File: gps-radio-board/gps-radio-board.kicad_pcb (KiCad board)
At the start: 4 copper layers, 25 x 54 mm, 45 parts, among them J1 SMA, J2 SMA, J3 USB_C_Receptacle_USB2.0_16P, J4 JST_BATT, J5 Conn_01x04, J6 Conn_01x04, J7 Conn_01x04, U1 ESP32-C6-MINI-1U-H4, U4 AP2112K-3.3, U5 MAX-M10N, U6 MCP73831, U7 AP2112K-3.3

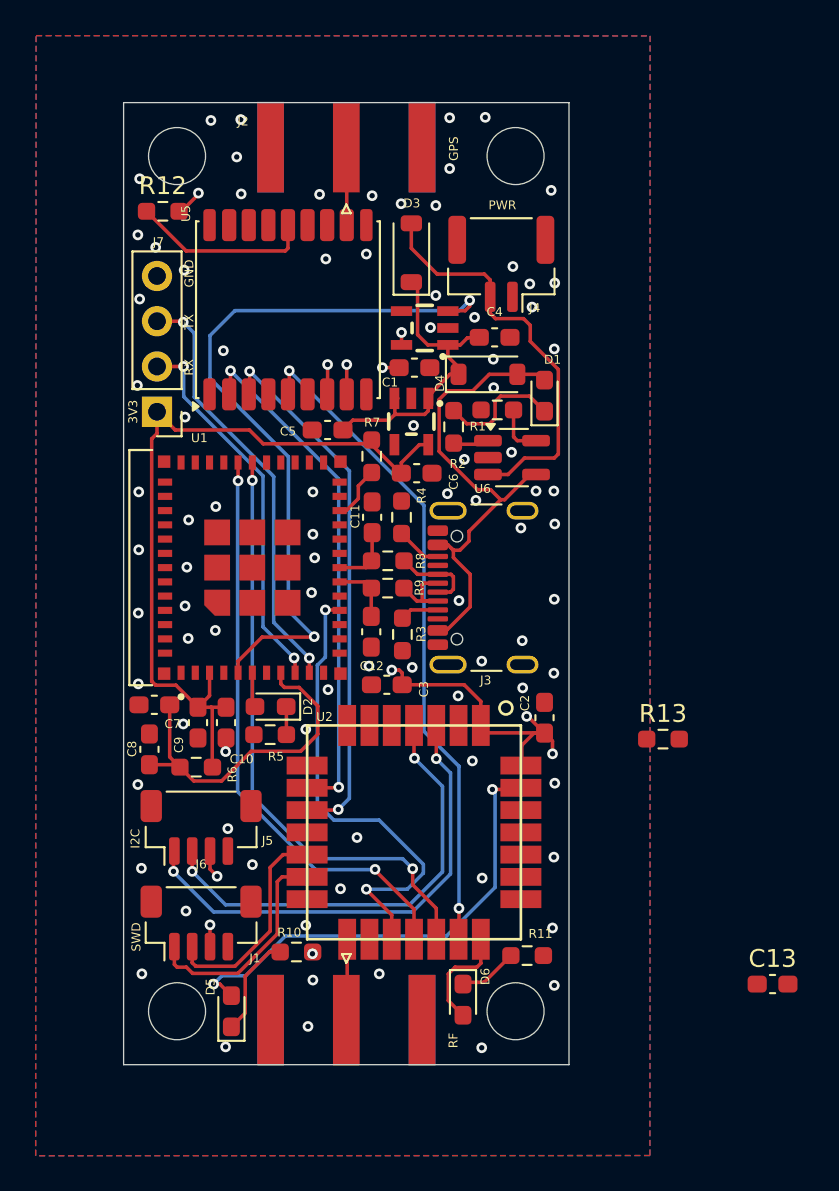
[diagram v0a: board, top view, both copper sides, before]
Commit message: Routing, mostly finished
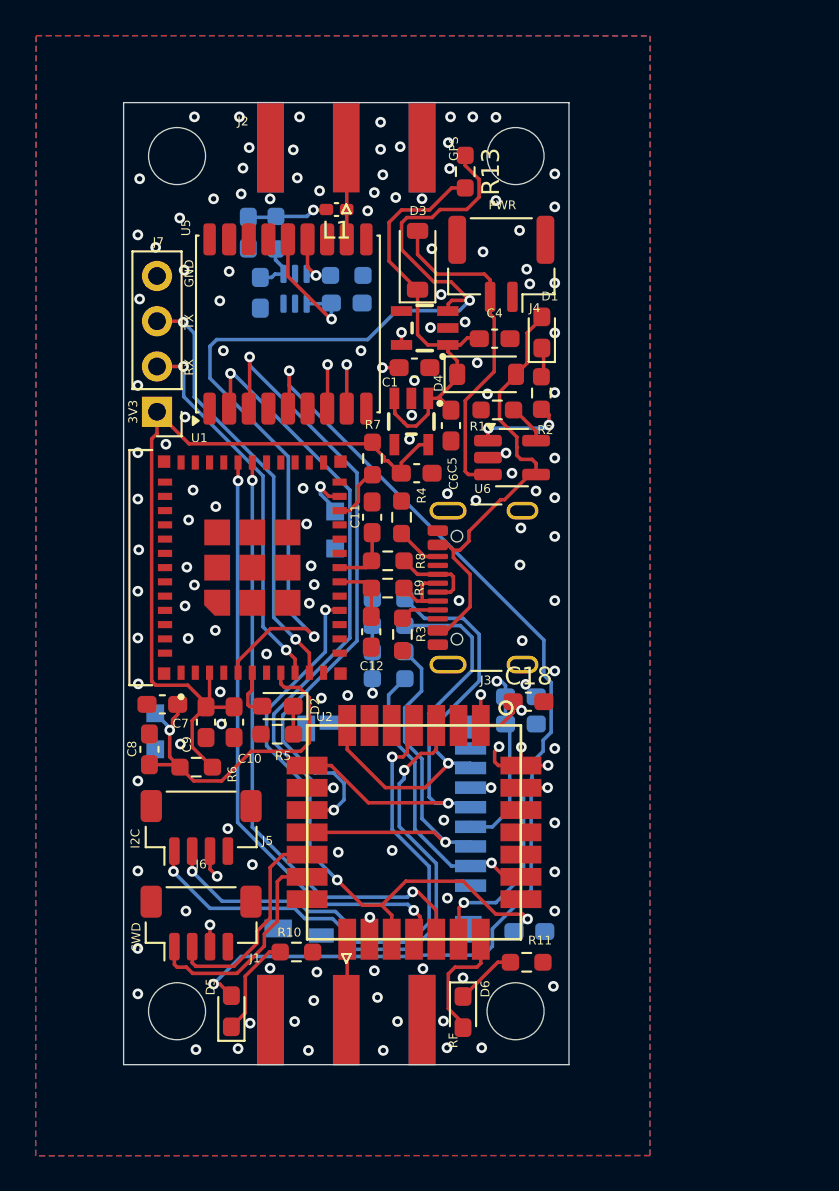
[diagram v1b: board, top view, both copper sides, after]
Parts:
- removed C2: 100n, Capacitor_SMD:C_0603_1608Metric_Pad1.08x0.95mm_HandSolder
- removed C3: 10u, Capacitor_SMD:C_0603_1608Metric_Pad1.08x0.95mm_HandSolder
- removed R12: 0, Resistor_SMD:R_0603_1608Metric_Pad0.98x0.95mm_HandSolder
- added BOOT1: TP2, TestPoint:TestPoint_Pad_1.0x1.0mm, B.Cu at (99.4, 96.0)
- added C14: 100n, Capacitor_SMD:C_0603_1608Metric_Pad1.08x0.95mm_HandSolder, B.Cu at (95.2, 83.7)
- added C15: 1u, Capacitor_SMD:C_0603_1608Metric_Pad1.08x0.95mm_HandSolder, B.Cu at (100.0, 84.2)
- added C16: 10n, Capacitor_SMD:C_0603_1608Metric_Pad1.08x0.95mm_HandSolder, B.Cu at (94.5, 80.3)
- added C17: 10u, Capacitor_SMD:C_0603_1608Metric_Pad1.08x0.95mm_HandSolder, B.Cu at (109.8, 106.3)
- added C18: 4.7u, Capacitor_SMD:C_0603_1608Metric_Pad1.08x0.95mm_HandSolder, F.Cu at (110.2, 106.6)
- added C19: 100n, Capacitor_SMD:C_0603_1608Metric_Pad1.08x0.95mm_HandSolder, B.Cu at (109.8, 107.9)
- added EN1: ESP_EN, TestPoint:TestPoint_Pad_1.0x1.0mm, B.Cu at (89.3, 109.3)
- added EN2: ESP_EN, TestPoint:TestPoint_Pad_1.0x1.0mm, B.Cu at (89.3, 107.3)
- added GND1: TP2, TestPoint:TestPoint_Pad_1.0x1.0mm, B.Cu at (99.4, 98.0)
- added J8: DM3CS-SF, Connector_Card:microSD_HC_Hirose_DM3D-SF, B.Cu at (101.6, 113.8)
- added L1: 27n, Inductor_SMD:L_0402_1005Metric_Pad0.77x0.64mm_HandSolder, F.Cu at (99.5, 79.0)
- added R14: 100k, Resistor_SMD:R_0603_1608Metric_Pad0.98x0.95mm_HandSolder, B.Cu at (100.0, 82.7)
- added R15: 10, Resistor_SMD:R_0603_1608Metric_Pad0.98x0.95mm_HandSolder, B.Cu at (96.0, 80.3)
- added R16: 10k, Resistor_SMD:R_0603_1608Metric_Pad0.98x0.95mm_HandSolder, B.Cu at (102.4, 105.3)
- added R17: 10k, Resistor_SMD:R_0603_1608Metric_Pad0.98x0.95mm_HandSolder, B.Cu at (102.4, 103.8)
- added R18: 10k, Resistor_SMD:R_0603_1608Metric_Pad0.98x0.95mm_HandSolder, B.Cu at (102.4, 100.8)
- added R19: 10k, Resistor_SMD:R_0603_1608Metric_Pad0.98x0.95mm_HandSolder, B.Cu at (102.4, 102.3)
- added U3: SiP32431DR3, Package_TO_SOT_SMD:SOT-363_SC-70-6, B.Cu at (97.1, 83.5)
- C13: moved to B.Cu
- moved R13 33.7 mm to (106.7, 76.9), turned to -90 degrees
- moved C13 14.0 mm to (110.3, 119.5)
- moved C5 6.93 mm to (105.9, 91.1), turned to -90 degrees
- moved R2 5.28 mm to (111.0, 89.3)
- moved D1 3.55 mm to (111.0, 85.9)
- moved U5 0.80 mm to (96.7, 85.4)
- moved D6 0.70 mm to (106.5, 124.0)
- moved D3 0.55 mm to (104.0, 81.8)
- moved C10 0.45 mm to (93.7, 107.8)
- moved C7 0.45 mm to (89.7, 106.8)
- moved C9 0.45 mm to (92.1, 107.8)
- moved D2 0.40 mm to (96.2, 106.9)
- moved R5 0.40 mm to (96.1, 108.5)
- moved R11 0.38 mm to (110.1, 121.2)
- moved R7 0.13 mm to (101.5, 93.0)
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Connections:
- U1 pad 23: unconnected-(U1-IO9-Pad23) -> Net-(U1-IO9)
- U2 pad 25: Net-(U2-PB9) -> unconnected-(U2-PB9-Pad25)
- U5 pad 13: Net-(U2-PB9) -> Net-(U3-ON)
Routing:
- net /SPI-SCK: track 0.00 -> 25.3 mm, vias 0 -> 1
- net /SPI-CITO: track 0.00 -> 23.3 mm, vias 0 -> 1
- net /SPI-COTI: track 0.00 -> 22.2 mm, vias 0 -> 1
- net /SPI-CS: track 0.00 -> 16.6 mm, vias 0 -> 1
- net Net-(U1-IO2): track 41.9 -> 56.2 mm
- net +3V3: track 26.2 -> 34.9 mm, vias 10 -> 13
- net Net-(U1-IO6): track 26.7 -> 34.9 mm, vias 2 -> 3
- net Net-(D3-K): track 18.7 -> 25.2 mm
- net /EXT_INT_GPS: track 37.2 -> 42.5 mm
- net Net-(D1-K): track 6.95 -> 1.62 mm
- net /WIO_UART_1_TX: track 30.2 -> 35.6 mm
- net /SWD-WIO-IO: track 27.1 -> 31.9 mm
- net Net-(C16-Pad2): track 0.00 -> 4.58 mm, vias 0 -> 1
- net +BATT: track 23.3 -> 18.9 mm
- net /SWD-WIO-CLK: track 25.6 -> 29.7 mm
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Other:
- board text added: "BOOT"
- board text added: "RST"

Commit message: Finish routing
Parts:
- moved C18 1.16 mm to (111.2, 107.3), turned to -90 degrees
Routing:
- net +3V3: track 34.9 -> 38.6 mm, vias 13 -> 14
- net +BATT: track 18.9 -> 21.0 mm
- net /EXT_INT_GPS: track 42.5 -> 43.2 mm
- net GND: vias 131 -> 135

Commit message: Small adjustments
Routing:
- net +3V3: track 38.6 -> 36.3 mm
- net Net-(U1-IO6): track 34.9 -> 35.6 mm
- net Net-(D3-K): track 25.2 -> 25.7 mm
- net GND: vias 135 -> 136

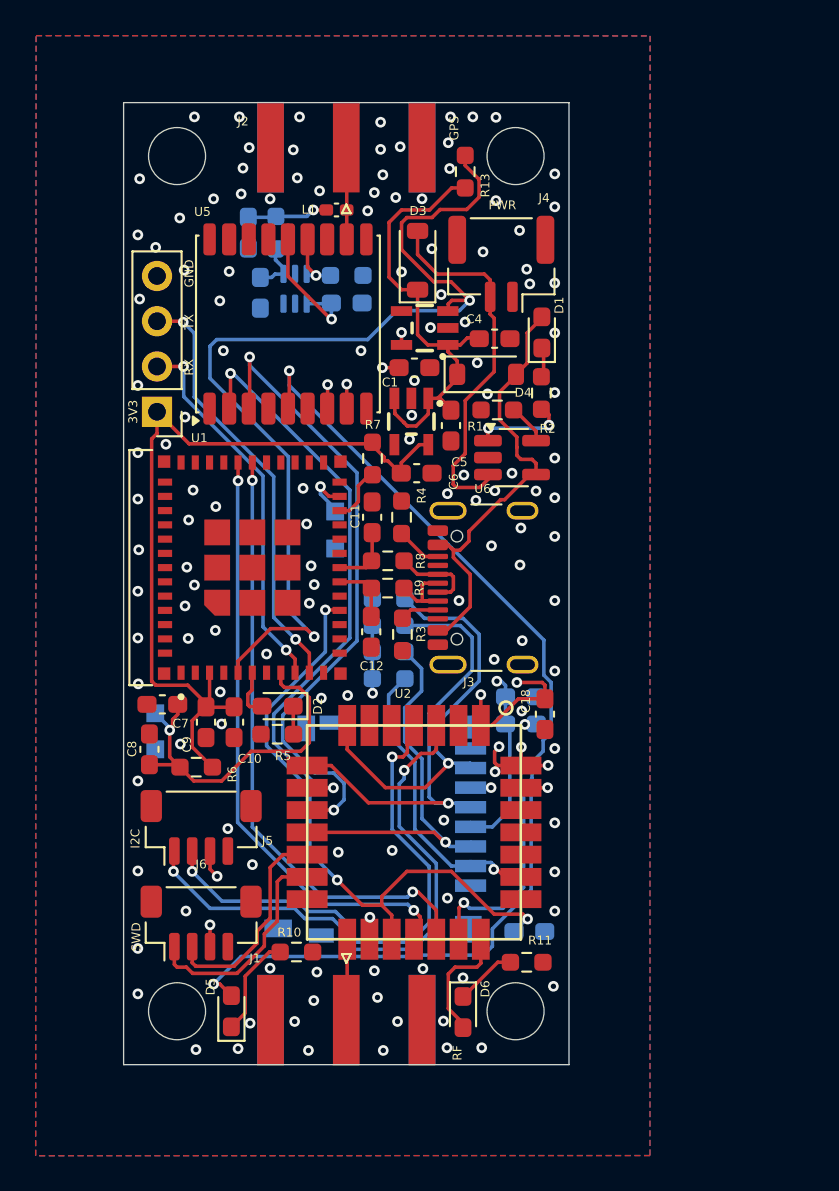
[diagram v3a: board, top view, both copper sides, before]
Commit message: Layout fixes. Swap 100k ref for en
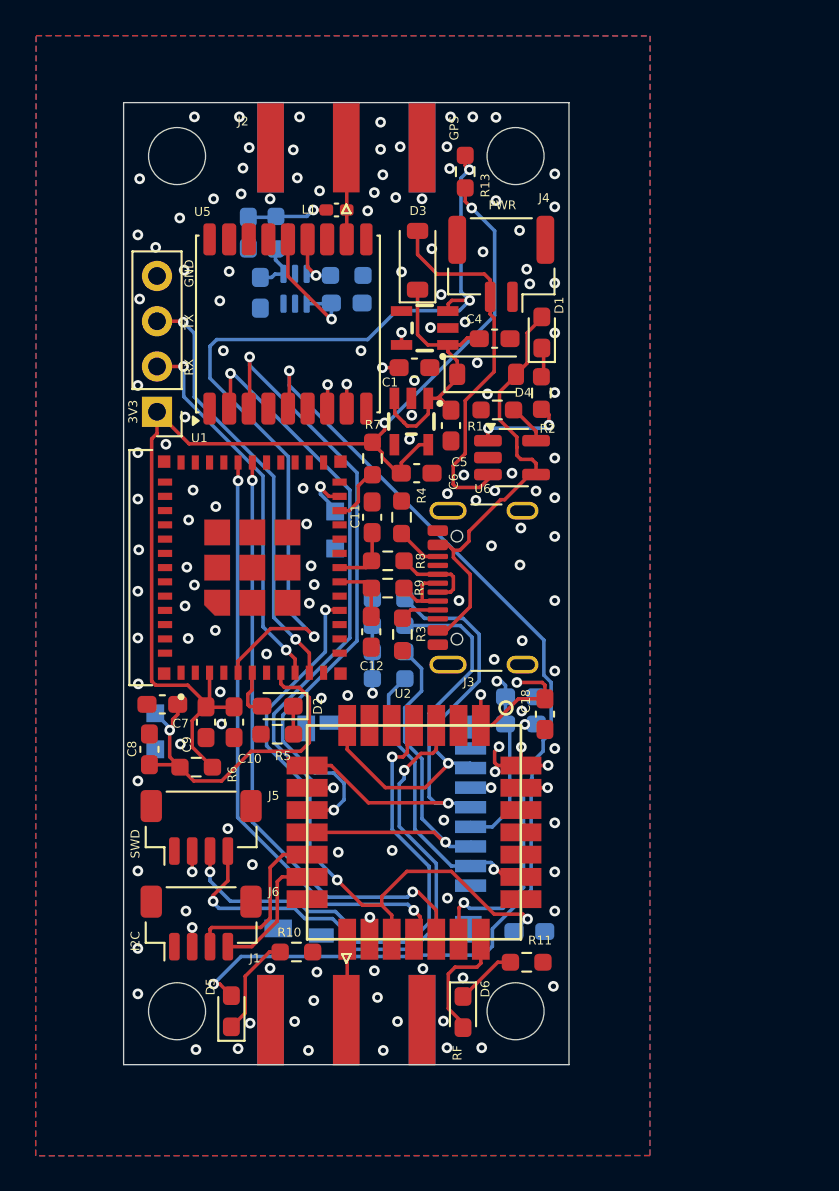
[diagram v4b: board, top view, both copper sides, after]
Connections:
- J5 pad 1: /SWD-WIO-IO -> GND
- J5 pad 2: /SWD-WIO-CLK -> +3V3
- J5 pad 3: +3V3 -> /SWD-WIO-CLK
- J5 pad 4: GND -> /SWD-WIO-IO
- J6 pad 1: /I2C-2-SCL -> GND
- J6 pad 2: /I2C-2-SCA -> +3V3
- J6 pad 3: +3V3 -> /I2C-2-SCA
- J6 pad 4: GND -> /I2C-2-SCL
- R13 pad 2: Net-(D3-K) -> +3V3_E
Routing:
- net +3V3_E: track 43.7 -> 61.7 mm, vias 0 -> 2
- net Net-(D3-K): track 25.7 -> 15.7 mm
- net Net-(U1-IO2): track 56.2 -> 50.7 mm, vias 2 -> 3
- net /I2C-2-SCL: track 12.6 -> 7.37 mm
- net /I2C-2-SCA: track 11.8 -> 9.83 mm
- net /SWD-WIO-IO: track 31.9 -> 31.1 mm
- net /SWD-WIO-CLK: track 29.7 -> 29.1 mm
- net +3V3: track 36.3 -> 35.7 mm

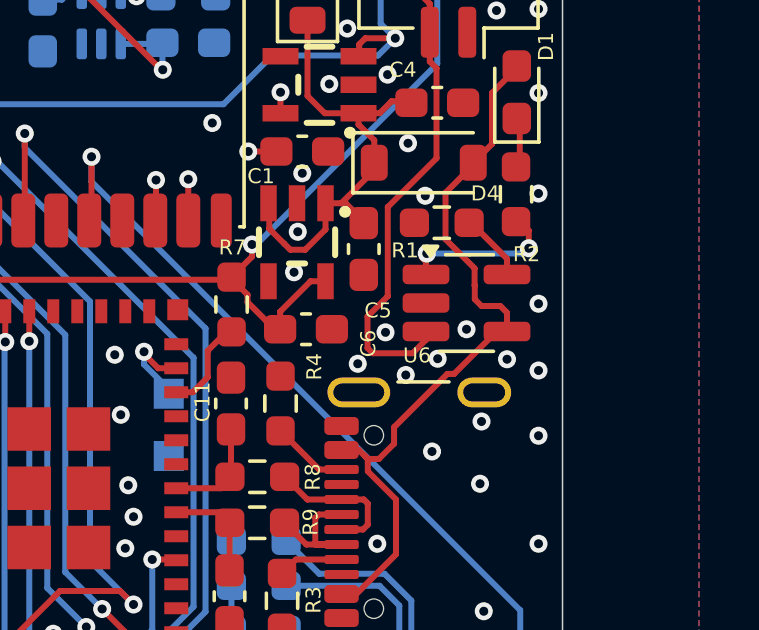
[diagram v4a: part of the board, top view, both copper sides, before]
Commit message: Add output cap for battery charger
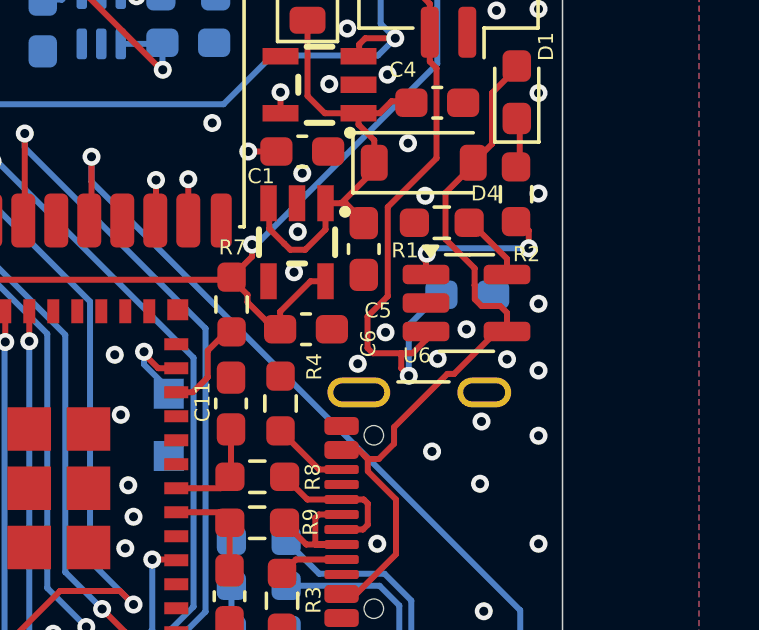
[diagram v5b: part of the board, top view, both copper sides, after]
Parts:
- added C20: 4.7u, Capacitor_SMD:C_0603_1608Metric_Pad1.08x0.95mm_HandSolder, B.Cu at (109.3, 92.7)
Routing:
- net +BATT: track 21.0 -> 25.1 mm, vias 0 -> 1
- net GND: vias 136 -> 135
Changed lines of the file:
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@@
 			(outputformat 1)
 			(mirror no)
-			(drillshape 1)
+			(drillshape 0)
 			(scaleselection 1)
-			(outputdirectory "")
+			(outputdirectory "gps-gerb/")
 		)
 	)
@@
 	(footprint "Capacitor_SMD:C_0603_1608Metric_Pad1.08x0.95mm_HandSolder"
 		(layer "B.Cu")
+		(at 109.325 92.65)
+		(descr "Capacitor SMD 0603 (1608 Metric), square (rectangular) end terminal, IPC-7351 nominal with elongated pad for handsoldering. (Body size source: IPC-SM-782 page 76, https://www.pcb-3d.com/wordpress/wp-content/uploads/ipc-sm-782a_amendment_1_and_2.pdf)")
+		(tags "capacitor handsolder")
+		(property "Reference" "C20"
+			(at 0.025 1.125 0)
+			(layer "B.SilkS")
+			(effects
+				(font
+					(size 0.5 0.5)
+					(thickness 0.07)
+				)
+				(justify mirror)
+			)
+		)
+		(property "Value" "4.7u"
+			(at 0 -1.43 0)
+			(layer "B.Fab")
+			(effects
+				(font
+					(size 1 1)
+					(thickness 0.15)
+				)
+				(justify mirror)
+			)
+		)
+		(property "Datasheet" ""
+			(at 0 0 0)
+			(layer "B.Fab")
+			(hide yes)
+			(effects
+				(font
+					(size 1.27 1.27)
+				)
+				(justify mirror)
+			)
+		)
+		(property "Description" "Unpolarized capacitor"
+			(at 0 0 0)
+			(layer "B.Fab")
+			(hide yes)
+			(effects
+				(font
+					(size 1.27 1.27)
+				)
+				(justify mirror)
+			)
+		)
+		(property ki_fp_filters "C_*")
+		(sheetname "/")
+		(sheetfile "gps-radio-board.kicad_sch")
+		(units
+			(unit
+				(name "A")
+				(pins "1" "2")
+			)
+		)
+		(attr smd)
+		(duplicate_pad_numbers_are_jumpers no)
+		(fp_line
+			(start -0.146267 -0.51)
+			(end 0.146267 -0.51)
+			(stroke
+				(width 0.12)
+				(type solid)
+			)
+			(layer "B.SilkS")
+		)
+		(fp_line
+			(start -0.146267 0.51)
+			(end 0.146267 0.51)
+			(stroke
+				(width 0.12)
+				(type solid)
+			)
+			(layer "B.SilkS")
+		)
+		(fp_rect
+			(start -1.65 0.73)
+			(end 1.65 -0.73)
+			(stroke
+				(width 0.05)
+				(type solid)
+			)
+			(fill no)
+			(layer "B.CrtYd")
+		)
+		(fp_rect
+			(start -0.8 0.4)
+			(end 0.8 -0.4)
+			(stroke
+				(width 0.1)
+				(type solid)
+			)
+			(fill no)
+			(layer "B.Fab")
+		)
+		(fp_text user "${REFERENCE}"
+			(at 0 0 0)
+			(layer "B.Fab")
+			(effects
+				(font
+					(size 0.4 0.4)
+					(thickness 0.06)
+				)
+				(justify mirror)
+			)
+		)
+		(pad "1" smd roundrect
+			(at -0.8625 0)
+			(size 1.075 0.95)
+			(layers "B.Cu" "B.Mask" "B.Paste")
+			(roundrect_rratio 0.25)
+			(net "+BATT")
+			(pintype "passive")
+		)
+		(pad "2" smd roundrect
+			(at 0.8625 0)
+			(size 1.075 0.95)
+			(layers "B.Cu" "B.Mask" "B.Paste")
+			(roundrect_rratio 0.25)
+			(net "GND")
+			(pintype "passive")
+		)
+		(embedded_fonts no)
+		(model "${KICAD10_3DMODEL_DIR}/Capacitor_SMD.3dshapes/C_0603_1608Metric.step"
+			(offset
+				(xyz 0 0 0)
+			)
+			(scale
+				(xyz 1 1 1)
+			)
+			(rotate
+				(xyz 0 0 0)
+			)
+		)
+	)
+	(footprint "Capacitor_SMD:C_0603_1608Metric_Pad1.08x0.95mm_HandSolder"
+		(layer "B.Cu")
 		(at 109.8 107.875)
 		(descr "Capacitor SMD 0603 (1608 Metric), square (rectangular) end terminal, IPC-7351 nominal with elongated pad for handsoldering. (Body size source: IPC-SM-782 page 76, https://www.pcb-3d.com/wordpress/wp-content/uploads/ipc-sm-782a_amendment_1_and_2.pdf)")
@@
 	)
 	(via
-		(at 107.275 95.325)
-		(size 0.6)
-		(drill 0.3)
-		(layers "F.Cu" "B.Cu")
-		(free yes)
-		(net "GND")
-	)
-	(via
 		(at 88.3 116.125)
 		(size 0.6)
@@
 	)
 	(segment
-		(start 111.15 91.275)
+		(start 108.15 91.1)
 		(end 111.325 91.1)
 		(width 0.2)
@@
 	(segment
 		(start 107.975 91.275)
-		(end 111.15 91.275)
+		(end 108.15 91.1)
 		(width 0.2)
 		(layer "B.Cu")
@@
 	)
 	(segment
+		(start 106.173529 94.6)
+		(end 107.125 94.6)
+		(width 0.2)
+		(layer "F.Cu")
+		(net "+BATT")
+	)
+	(segment
 		(start 104 81.525)
 		(end 105.1 82.625)
@@
 	)
 	(segment
-		(start 106.173529 94.6)
+		(start 107.125 95.1)
+		(end 107.35 95.325)
+		(width 0.2)
+		(layer "F.Cu")
+		(net "+BATT")
+	)
+	(segment
+		(start 107.125 94.6)
+		(end 107.125 95.1)
+		(width 0.2)
+		(layer "F.Cu")
+		(net "+BATT")
+	)
+	(segment
+		(start 107.125 94.6)
 		(end 107.5 94.6)
 		(width 0.2)
@@
 		(net "+BATT")
 	)
+	(via
+		(at 107.375 95.35)
+		(size 0.6)
+		(drill 0.3)
+		(layers "F.Cu" "B.Cu")
+		(net "+BATT")
+	)
+	(segment
+		(start 108.5125 92.525)
+		(end 107.375 93.6625)
+		(width 0.2)
+		(layer "B.Cu")
+		(net "+BATT")
+	)
+	(segment
+		(start 107.375 93.6625)
+		(end 107.375 95.35)
+		(width 0.2)
+		(layer "B.Cu")
+		(net "+BATT")
+	)
